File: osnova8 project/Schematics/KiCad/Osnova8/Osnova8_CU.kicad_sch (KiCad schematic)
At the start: 8 parts, among them U35 74LS161, U36 74LS08, U37 74LS138, U38 74LS08, U39 74LS08

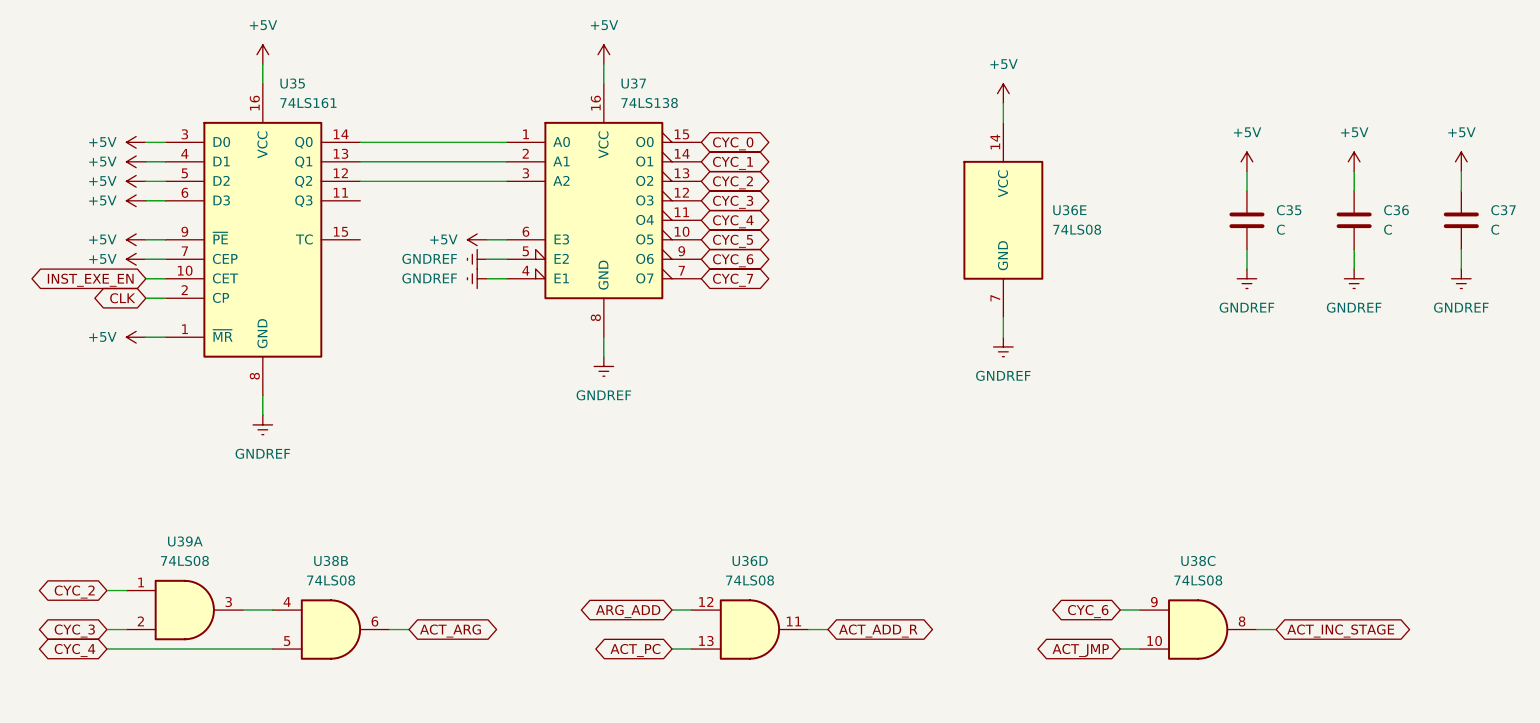
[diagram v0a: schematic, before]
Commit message: updated schematics
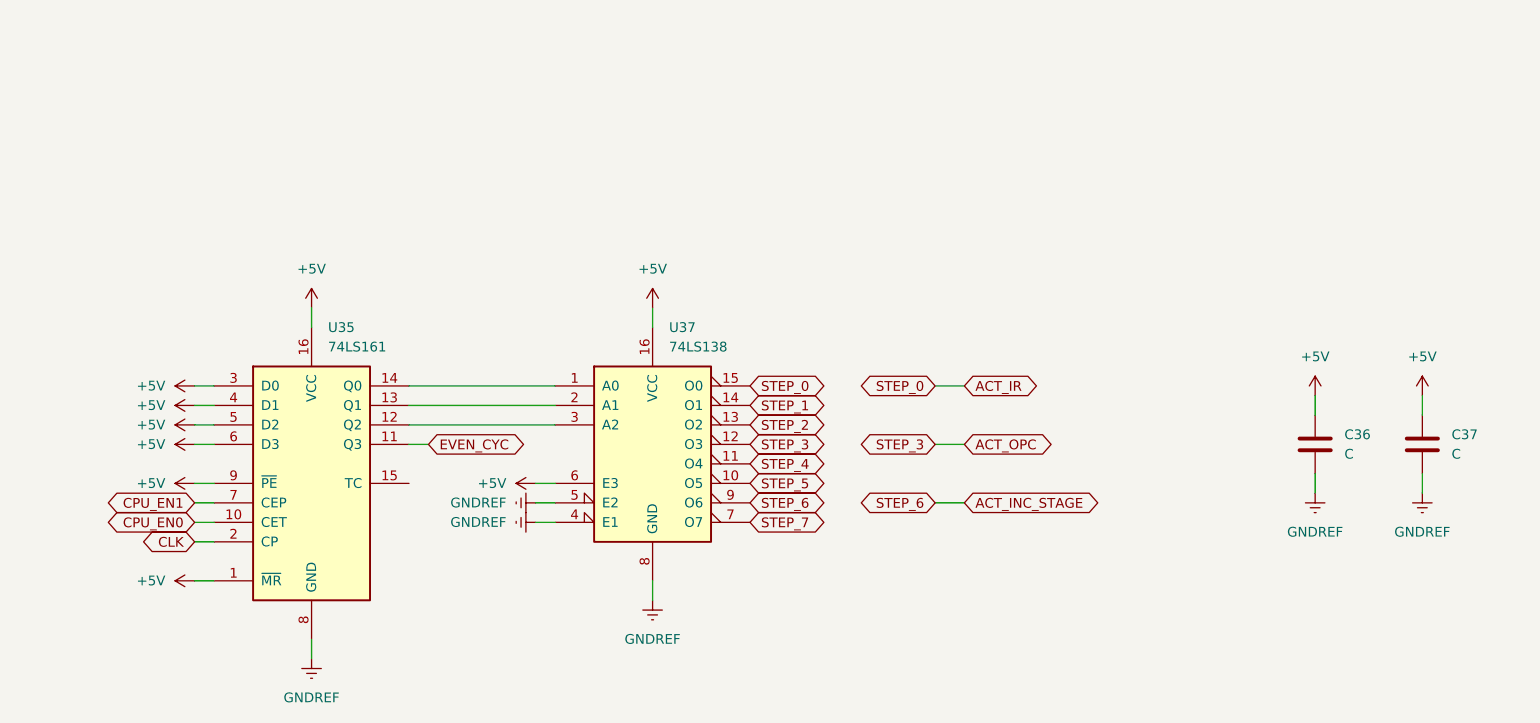
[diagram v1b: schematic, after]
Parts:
- removed C35: C, symbol Device:C
- removed U36, U38, U39: 74LS08, symbol 74xx:74LS08
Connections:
- net CYC_6 is gone; now on net ACT_INC_STAGE: U37.9 (O6)
- net +5V: no longer U35.7 (CEP)
- net EVEN_CYC: now reaches U35.11 (Q3)
- net CYC_0 renamed ACT_IR
- net CYC_1 renamed STEP_1
- net CYC_2 renamed STEP_2
- net CYC_3 renamed ACT_OPC
- net CYC_4 renamed STEP_4
- net CYC_5 renamed STEP_5
- net CYC_7 renamed STEP_7
- net INST_EXE_EN renamed CPU_EN0
- new net CPU_EN1: U35.7 (CEP)
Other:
- moved on the sheet: C36, C37, U35, U37
